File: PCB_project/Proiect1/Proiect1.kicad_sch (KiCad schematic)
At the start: 38 parts, among them J1 OUT, J2 +25V, J3 GND, Q1 BC846, Q10 BC846, Q11 BC846, Q12 BC856, Q13 BC856, Q2 BC856, Q3 BC856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

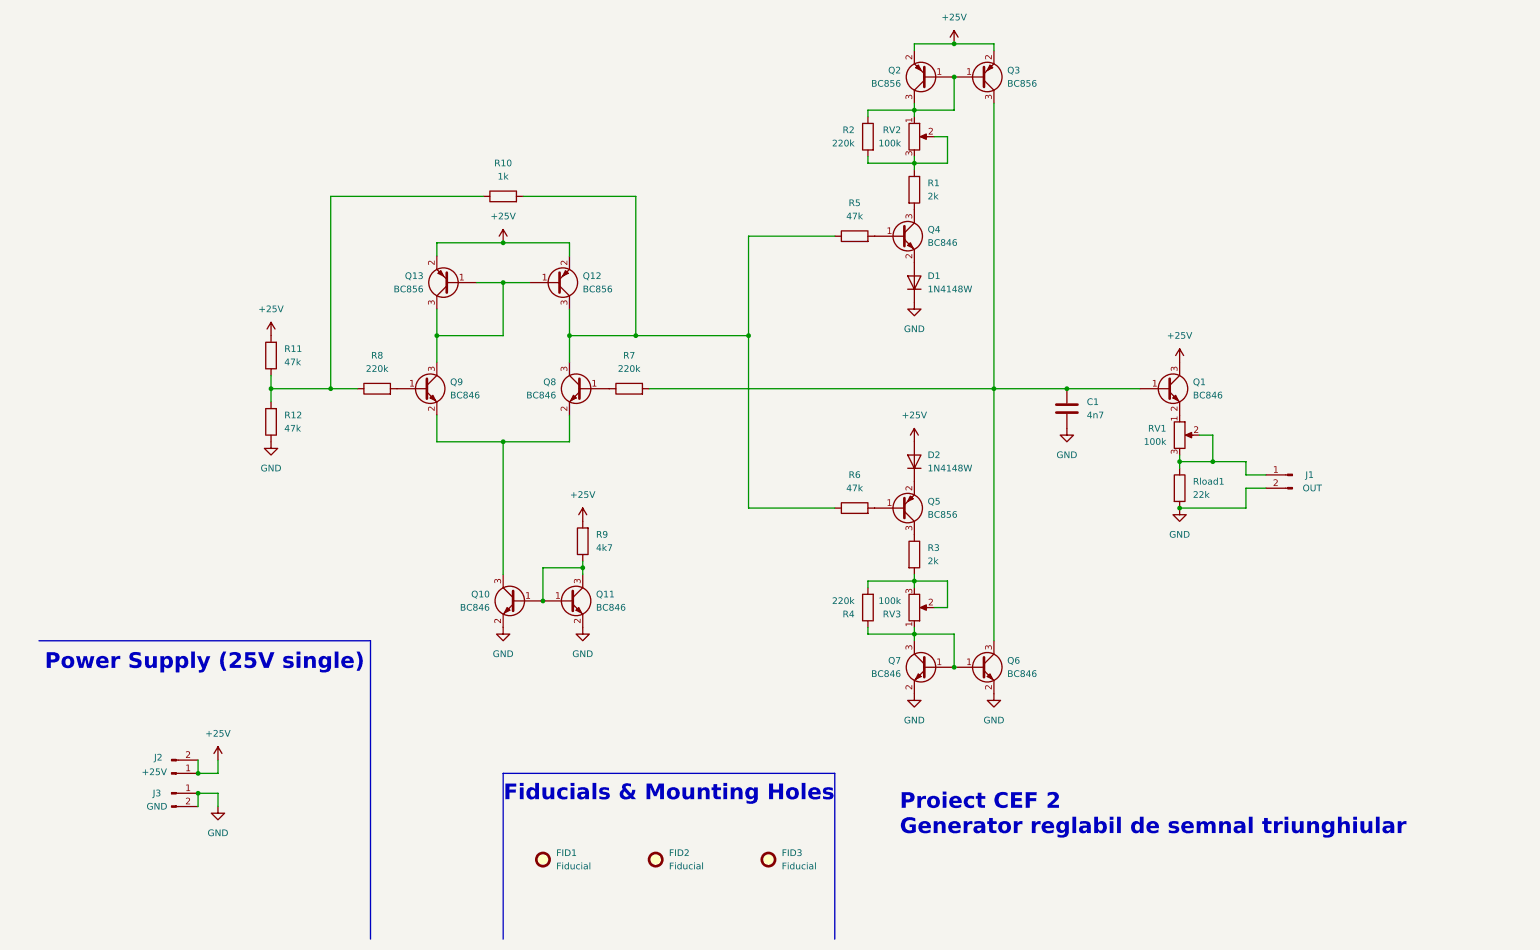
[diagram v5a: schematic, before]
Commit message: Changed footprints of header pins for Power and Output
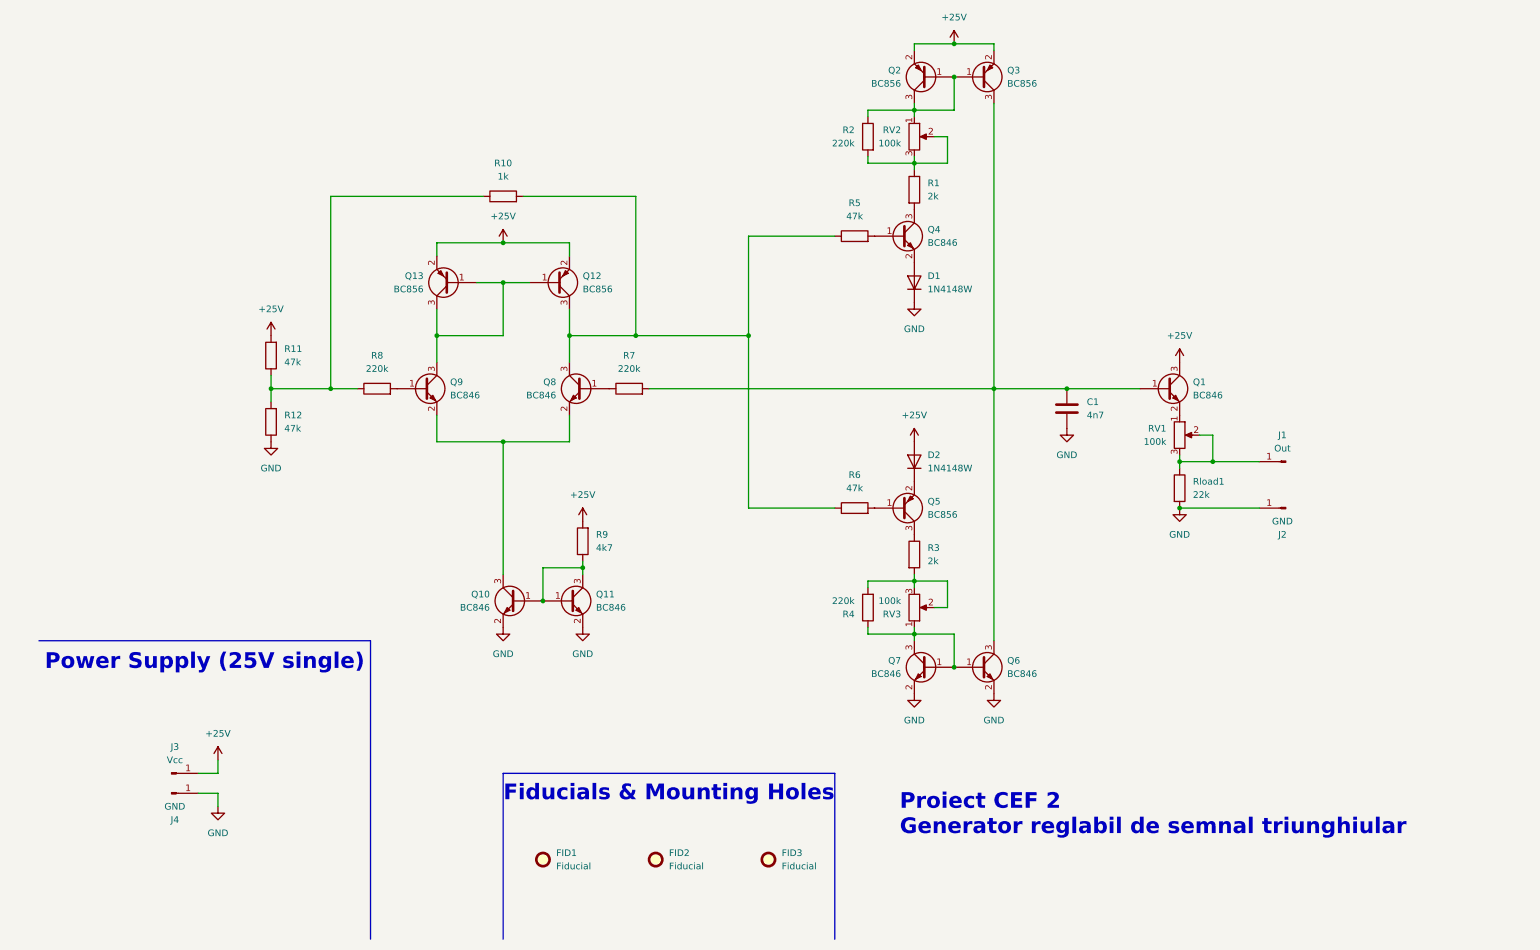
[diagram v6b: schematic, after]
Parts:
- removed J1: OUT, Connector_PinHeader_2.00mm:PinHeader_1x02_P2.00mm_Vertical_SMD_Pin1Left, symbol Connector:Conn_01x02_Pin
- removed J2: +25V, Connector_PinHeader_2.00mm:PinHeader_1x02_P2.00mm_Vertical_SMD_Pin1Left, symbol Connector:Conn_01x02_Pin
- removed J3: GND, Connector_PinHeader_2.00mm:PinHeader_1x02_P2.00mm_Vertical_SMD_Pin1Left, symbol Connector:Conn_01x02_Pin
- added J1: Out, TestPoint:TestPoint_Pad_2.0x2.0mm, symbol Connector:Conn_01x01_Pin
- added J2, J4: GND, TestPoint:TestPoint_Pad_2.0x2.0mm, symbol Connector:Conn_01x01_Pin
- added J3: Vcc, TestPoint:TestPoint_Pad_2.0x2.0mm, symbol Connector:Conn_01x01_Pin
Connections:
- net +25V: now also J3.1 (Pin_1)
- net GND: now also J2.1 (Pin_1), J4.1 (Pin_1)
- net at RV1.2, RV1.3, Rload1.1: now also J1.1 (Pin_1)
